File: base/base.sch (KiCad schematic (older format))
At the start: 22 parts, among them J1 USB_OTG, SW1 SW_Push, U1 Z80CPU, U2 27C256, U3 7404, U4 55257, U5 7432, U6 16550, U7 FT230XS, X1 4 MHz

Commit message: Layout work
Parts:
- added J2: CONN_02X20, Pin_Headers:Pin_Header_Straight_2x20_Pitch2.54mm, symbol CONN_02X20
- added unit 4 of U3
- added unit 3 of U5
- added X2: 1.8432 MHz, Oscillators:Oscillator_DIP-8, symbol CXO_DIP8
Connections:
- net labels added: IORQ, UART_CE
- wire segments 161 -> 223
- no-connect marks 2 -> 4
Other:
- moved on the sheet: C3, D1, R1, SW1, U3A, U3B

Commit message: Replaced SMD passives with THT
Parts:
- C1, C2, C4, C5, C6, C7, C8: footprint Capacitors_SMD:C_0805 -> Capacitors_THT:C_Disc_D4.3mm_W1.9mm_P5.00mm
- C3: footprint Capacitors_SMD:CP_Elec_4x4.5 -> Capacitors_THT:CP_Radial_D5.0mm_P2.50mm
- D1: footprint Diodes_SMD:D_SOD-523 -> Diodes_THT:D_A-405_P7.62mm_Horizontal
- R1, R2, R3: footprint Resistors_SMD:R_0805 -> Resistors_THT:R_Axial_DIN0207_L6.3mm_D2.5mm_P10.16mm_Horizontal
- SW1: footprint Buttons_Switches_SMD:SW_SPST_TL3342 -> Buttons_Switches_THT:SW_PUSH_6mm_h5mm
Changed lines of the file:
@@
 F 0 "C1" H 2592 2246 50  0000 L CNN
 F 1 "1 uF" H 2592 2155 50  0000 L CNN
-F 2 "Capacitors_SMD:C_0805" H 2500 2200 50  0001 C CNN
+F 2 "Capacitors_THT:C_Disc_D4.3mm_W1.9mm_P5.00mm" H 2500 2200 50  0001 C CNN
 F 3 "" H 2500 2200 50  0001 C CNN
 	1    2500 2200
@@
 F 0 "C2" H 5342 2396 50  0000 L CNN
 F 1 "1 uF" H 5342 2305 50  0000 L CNN
-F 2 "Capacitors_SMD:C_0805" H 5250 2350 50  0001 C CNN
+F 2 "Capacitors_THT:C_Disc_D4.3mm_W1.9mm_P5.00mm" H 5250 2350 50  0001 C CNN
 F 3 "" H 5250 2350 50  0001 C CNN
 	1    5250 2350
@@
 F 0 "SW1" H 1000 10585 50  0000 C CNN
 F 1 "SW_Push" H 1000 10494 50  0000 C CNN
-F 2 "Buttons_Switches_SMD:SW_SPST_TL3342" H 1000 10500 50  0001 C CNN
+F 2 "Buttons_Switches_THT:SW_PUSH_6mm_h5mm" H 1000 10500 50  0001 C CNN
 F 3 "" H 1000 10500 50  0001 C CNN
 	1    1000 10300
@@
 F 0 "R1" H 1559 9996 50  0000 L CNN
 F 1 "10k" H 1559 9905 50  0000 L CNN
-F 2 "Resistors_SMD:R_0805" H 1500 9950 50  0001 C CNN
+F 2 "Resistors_THT:R_Axial_DIN0207_L6.3mm_D2.5mm_P10.16mm_Horizontal" H 1500 9950 50  0001 C CNN
 F 3 "" H 1500 9950 50  0001 C CNN
 	1    1500 9950
@@
 F 0 "C3" H 1291 10596 50  0000 L CNN
 F 1 "47 uF" H 1291 10505 50  0000 L CNN
-F 2 "Capacitors_SMD:CP_Elec_4x4.5" H 1200 10550 50  0001 C CNN
+F 2 "Capacitors_THT:CP_Radial_D5.0mm_P2.50mm" H 1200 10550 50  0001 C CNN
 F 3 "" H 1200 10550 50  0001 C CNN
 	1    1200 10550
@@
 F 0 "C4" H 7592 2446 50  0000 L CNN
 F 1 "1 uF" H 7592 2355 50  0000 L CNN
-F 2 "Capacitors_SMD:C_0805" H 7500 2400 50  0001 C CNN
+F 2 "Capacitors_THT:C_Disc_D4.3mm_W1.9mm_P5.00mm" H 7500 2400 50  0001 C CNN
 F 3 "" H 7500 2400 50  0001 C CNN
 	1    7500 2400
@@
 F 0 "C5" H 9892 2346 50  0000 L CNN
 F 1 "C_Small" H 9892 2255 50  0000 L CNN
-F 2 "Capacitors_SMD:C_0805" H 9800 2300 50  0001 C CNN
+F 2 "Capacitors_THT:C_Disc_D4.3mm_W1.9mm_P5.00mm" H 9800 2300 50  0001 C CNN
 F 3 "" H 9800 2300 50  0001 C CNN
 	1    9800 2300
@@
 F 0 "D1" H 1350 9484 50  0000 C CNN
 F 1 "1N4148" H 1350 9575 50  0000 C CNN
-F 2 "Diodes_SMD:D_SOD-523" H 1350 9525 50  0001 C CNN
+F 2 "Diodes_THT:D_A-405_P7.62mm_Horizontal" H 1350 9525 50  0001 C CNN
 F 3 "" H 1350 9700 50  0001 C CNN
 	1    1350 9700
@@
 F 0 "R2" V 12700 3050 50  0000 C CNN
 F 1 "27" V 12700 3200 50  0000 C CNN
-F 2 "Resistors_SMD:R_0805" H 12800 3100 50  0001 C CNN
+F 2 "Resistors_THT:R_Axial_DIN0207_L6.3mm_D2.5mm_P10.16mm_Horizontal" H 12800 3100 50  0001 C CNN
 F 3 "" H 12800 3100 50  0001 C CNN
 	1    12800 3100
@@
 F 0 "R3" V 12700 3250 50  0000 C CNN
 F 1 "27" V 12700 3100 50  0000 C CNN
-F 2 "Resistors_SMD:R_0805" H 12800 3200 50  0001 C CNN
+F 2 "Resistors_THT:R_Axial_DIN0207_L6.3mm_D2.5mm_P10.16mm_Horizontal" H 12800 3200 50  0001 C CNN
 F 3 "" H 12800 3200 50  0001 C CNN
 	1    12800 3200
@@
 F 0 "C8" V 12621 2800 50  0000 C CNN
 F 1 "100 nF" V 12712 2800 50  0000 C CNN
-F 2 "Capacitors_SMD:C_0805" H 12850 2800 50  0001 C CNN
+F 2 "Capacitors_THT:C_Disc_D4.3mm_W1.9mm_P5.00mm" H 12850 2800 50  0001 C CNN
 F 3 "" H 12850 2800 50  0001 C CNN
 	1    12850 2800
@@
 F 0 "C6" H 12492 3496 50  0000 L CNN
 F 1 "47 nF" H 12492 3405 50  0000 L CNN
-F 2 "Capacitors_SMD:C_0805" H 12400 3450 50  0001 C CNN
+F 2 "Capacitors_THT:C_Disc_D4.3mm_W1.9mm_P5.00mm" H 12400 3450 50  0001 C CNN
 F 3 "" H 12400 3450 50  0001 C CNN
 	1    12400 3450
@@
 F 0 "C7" H 12692 3496 50  0000 L CNN
 F 1 "47 nF" H 12692 3405 50  0000 L CNN
-F 2 "Capacitors_SMD:C_0805" H 12600 3450 50  0001 C CNN
+F 2 "Capacitors_THT:C_Disc_D4.3mm_W1.9mm_P5.00mm" H 12600 3450 50  0001 C CNN
 F 3 "" H 12600 3450 50  0001 C CNN
 	1    12600 3450

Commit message: Further layout work
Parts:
- removed C2, C4: 1 uF, Capacitors_THT:C_Disc_D4.3mm_W1.9mm_P5.00mm, symbol C_Small
- removed C6, C7: 47 nF, Capacitors_THT:C_Disc_D4.3mm_W1.9mm_P5.00mm, symbol C_Small
- removed C8: 100 nF, Capacitors_THT:C_Disc_D4.3mm_W1.9mm_P5.00mm, symbol C_Small
- removed J1: USB_OTG, Connectors_USB:USB_Micro-B_Molex-105017-0001, symbol USB_OTG
- removed J2: CONN_02X20, Pin_Headers:Pin_Header_Straight_2x20_Pitch2.54mm, symbol CONN_02X20
- removed R2, R3: 27, Resistors_THT:R_Axial_DIN0207_L6.3mm_D2.5mm_P10.16mm_Horizontal, symbol R_Small
- removed U7: FT230XS, SMD_Packages:SO-16-L, symbol FT230XS
- added J1: FTDI, symbol CONN_01X06
- added JP1: CLK JMP, symbol Jumper_NC_Small
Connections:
- net labels added: CTS, INT, RTS, RX, TX
- wire segments 223 -> 174
- no-connect marks 4 -> 3

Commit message: Added RC2014 header to schematic
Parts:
- added J?: CONN_01X40, symbol CONN_01X40
- added J?: CONN_01X04, symbol CONN_01X04
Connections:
- net +5V: now also J?.18 (P18)
- net A0: now also J?.16 (P16)
- net A1: now also J?.15 (P15)
- net A10: now also J?.6 (P6)
- net A11: now also J?.5 (P5)
- net A12: now also J?.4 (P4)
- net A13: now also J?.3 (P3)
- net A14: now also J?.2 (P2)
- net A15: now also J?.1 (P1)
- net A2: now also J?.14 (P14)
- net A3: now also J?.13 (P13)
- net A4: now also J?.12 (P12)
- net A5: now also J?.11 (P11)
- net A6: now also J?.10 (P10)
- net A7: now also J?.9 (P9)
- net A8: now also J?.8 (P8)
- net A9: now also J?.7 (P7)
- net D0: now also J?.27 (P27)
- net D1: now also J?.28 (P28)
- net D2: now also J?.29 (P29)
- net D3: now also J?.30 (P30)
- net D4: now also J?.31 (P31)
- net D5: now also J?.32 (P32)
- net D6: now also J?.33 (P33)
- net D7: now also J?.34 (P34)
- net GND: now also J?.17 (P17)
- net INT: now also J?.22 (P22)
- net IORQ: now also J?.26 (P26)
- net MREQ: now also J?.23 (P23)
- net RD: now also J?.25 (P25)
- net RESET: now also J?.20 (P20)
- net RX: now also J?.36 (P36)
- net TX: now also J?.35 (P35)
- net WR: now also J?.24 (P24)
- net M1: now reaches U1.27 (~M1~)
- net M1: now also J?.19 (P19)
- net CLOCK: now reaches JP1.2, U1.6 (~CLK~)
- net CLOCK: now also J?.21 (P21)
- new net: J?.37 (P37), J?.4 (P4)
- new net: J?.3 (P3), J?.38 (P38)
- new net: J?.2 (P2), J?.39 (P39)
- new net: J?.1 (P1), J?.40 (P40)
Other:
- moved on the sheet: C3, D1, R1, SW1, U3A, U3B

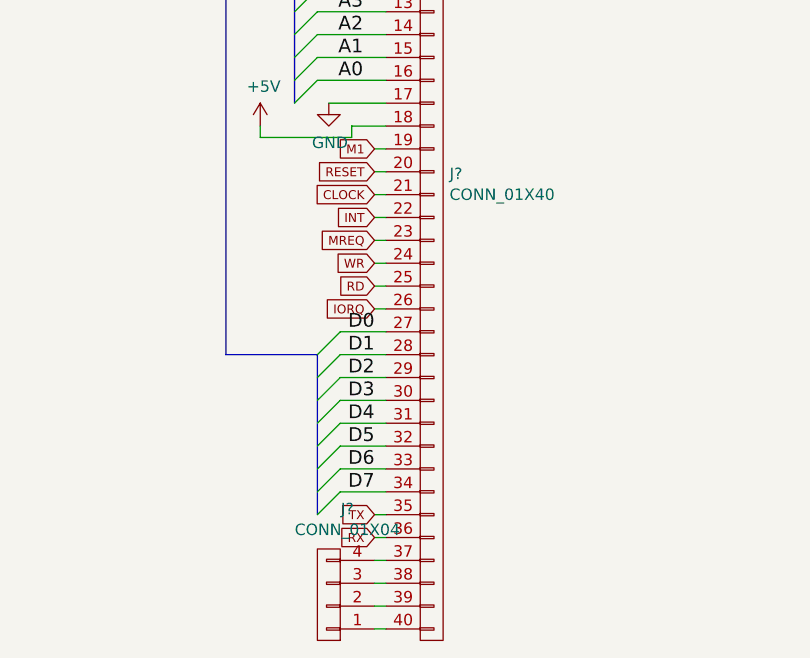
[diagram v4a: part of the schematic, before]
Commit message: Changed FTDI and CLK_JMP footprint
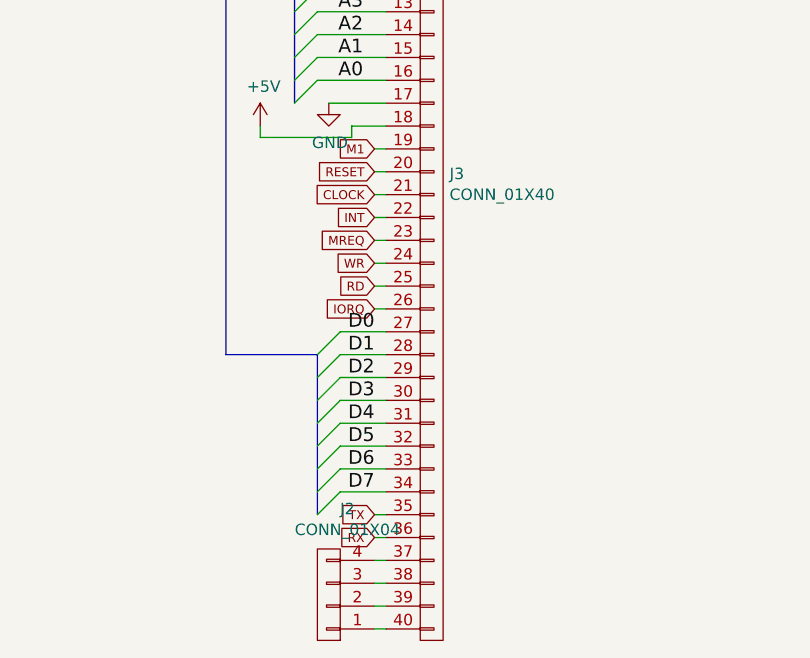
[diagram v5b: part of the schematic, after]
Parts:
- J1: footprint (none) -> Pin_Headers:Pin_Header_Straight_1x06_Pitch2.54mm
- J2: renamed from J?; footprint (none) -> Pin_Headers:Pin_Header_Straight_1x04_Pitch2.54mm
- J3: renamed from J?; footprint (none) -> Pin_Headers:Pin_Header_Straight_1x40_Pitch2.54mm
- JP1: footprint (none) -> Pin_Headers:Pin_Header_Straight_1x02_Pitch2.54mm
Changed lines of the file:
@@
 	6150 3350 6250 3450
 $Comp
-L GND #PWR9
+L GND #PWR01
 U 1 1 5966AA78
 P 2500 5500
-F 0 "#PWR9" H 2500 5250 50  0001 C CNN
+F 0 "#PWR01" H 2500 5250 50  0001 C CNN
 F 1 "GND" H 2505 5327 50  0000 C CNN
 F 2 "" H 2500 5500 50  0001 C CNN
@@
 $EndComp
 $Comp
-L +5V #PWR8
+L +5V #PWR02
 U 1 1 5966ABCC
 P 2500 2000
-F 0 "#PWR8" H 2500 1850 50  0001 C CNN
+F 0 "#PWR02" H 2500 1850 50  0001 C CNN
 F 1 "+5V" H 2515 2173 50  0000 C CNN
 F 2 "" H 2500 2000 50  0001 C CNN
@@
 $EndComp
 $Comp
-L GND #PWR11
+L GND #PWR03
 U 1 1 5966AD0D
 P 5250 4650
-F 0 "#PWR11" H 5250 4400 50  0001 C CNN
+F 0 "#PWR03" H 5250 4400 50  0001 C CNN
 F 1 "GND" H 5255 4477 50  0000 C CNN
 F 2 "" H 5250 4650 50  0001 C CNN
@@
 $EndComp
 $Comp
-L +5V #PWR10
+L +5V #PWR04
 U 1 1 5966ADF6
 P 5250 2150
-F 0 "#PWR10" H 5250 2000 50  0001 C CNN
+F 0 "#PWR04" H 5250 2000 50  0001 C CNN
 F 1 "+5V" H 5265 2323 50  0000 C CNN
 F 2 "" H 5250 2150 50  0001 C CNN
@@
 $EndComp
 $Comp
-L +5V #PWR2
+L +5V #PWR05
 U 1 1 5966B631
 P 950 2600
-F 0 "#PWR2" H 950 2450 50  0001 C CNN
+F 0 "#PWR05" H 950 2450 50  0001 C CNN
 F 1 "+5V" H 965 2773 50  0000 C CNN
 F 2 "" H 950 2600 50  0001 C CNN
@@
 NoConn ~ 650  3000
 $Comp
-L GND #PWR3
+L GND #PWR06
 U 1 1 5966B6FC
 P 950 3400
-F 0 "#PWR3" H 950 3150 50  0001 C CNN
+F 0 "#PWR06" H 950 3150 50  0001 C CNN
 F 1 "GND" H 955 3227 50  0000 C CNN
 F 2 "" H 950 3400 50  0001 C CNN
@@
 $EndComp
 $Comp
-L GND #PWR1
+L GND #PWR07
 U 1 1 5966D26A
 P 12150 8950
-F 0 "#PWR1" H 12150 8700 50  0001 C CNN
+F 0 "#PWR07" H 12150 8700 50  0001 C CNN
 F 1 "GND" H 12155 8777 50  0000 C CNN
 F 2 "" H 12150 8950 50  0001 C CNN
@@
 $EndComp
 $Comp
-L +5V #PWR5
+L +5V #PWR08
 U 1 1 5966D324
 P 13050 8150
-F 0 "#PWR5" H 13050 8000 50  0001 C CNN
+F 0 "#PWR08" H 13050 8000 50  0001 C CNN
 F 1 "+5V" H 13065 8323 50  0000 C CNN
 F 2 "" H 13050 8150 50  0001 C CNN
@@
 ~RESET~
 $Comp
-L GND #PWR4
+L GND #PWR09
 U 1 1 5966DD94
 P 12650 9300
-F 0 "#PWR4" H 12650 9050 50  0001 C CNN
+F 0 "#PWR09" H 12650 9050 50  0001 C CNN
 F 1 "GND" H 12655 9127 50  0000 C CNN
 F 2 "" H 12650 9300 50  0001 C CNN
@@
 $EndComp
 $Comp
-L GND #PWR7
+L GND #PWR010
 U 1 1 5966E3B1
 P 13500 9200
-F 0 "#PWR7" H 13500 8950 50  0001 C CNN
+F 0 "#PWR010" H 13500 8950 50  0001 C CNN
 F 1 "GND" H 13505 9027 50  0000 C CNN
 F 2 "" H 13500 9200 50  0001 C CNN
@@
 $EndComp
 $Comp
-L +5V #PWR6
+L +5V #PWR011
 U 1 1 5966E548
 P 13500 8500
-F 0 "#PWR6" H 13500 8350 50  0001 C CNN
+F 0 "#PWR011" H 13500 8350 50  0001 C CNN
 F 1 "+5V" H 13515 8673 50  0000 C CNN
 F 2 "" H 13500 8500 50  0001 C CNN
@@
 $EndComp
 $Comp
-L +5V #PWR12
+L +5V #PWR012
 U 1 1 5967000D
 P 7500 2200
-F 0 "#PWR12" H 7500 2050 50  0001 C CNN
+F 0 "#PWR012" H 7500 2050 50  0001 C CNN
 F 1 "+5V" H 7515 2373 50  0000 C CNN
 F 2 "" H 7500 2200 50  0001 C CNN
@@
 $EndComp
 $Comp
-L GND #PWR13
+L GND #PWR013
 U 1 1 5967079F
 P 7500 4700
-F 0 "#PWR13" H 7500 4450 50  0001 C CNN
+F 0 "#PWR013" H 7500 4450 50  0001 C CNN
 F 1 "GND" H 7505 4527 50  0000 C CNN
 F 2 "" H 7500 4700 50  0001 C CNN
@@
 $EndComp
 $Comp
-L +5V #PWR18
+L +5V #PWR014
 U 1 1 5967680A
 P 9800 2100
-F 0 "#PWR18" H 9800 1950 50  0001 C CNN
+F 0 "#PWR014" H 9800 1950 50  0001 C CNN
 F 1 "+5V" H 9815 2273 50  0000 C CNN
 F 2 "" H 9800 2100 50  0001 C CNN
@@
 $EndComp
 $Comp
-L GND #PWR19
+L GND #PWR015
 U 1 1 59676BF3
 P 9800 6000
-F 0 "#PWR19" H 9800 5750 50  0001 C CNN
+F 0 "#PWR015" H 9800 5750 50  0001 C CNN
 F 1 "GND" H 9805 5827 50  0000 C CNN
 F 2 "" H 9800 6000 50  0001 C CNN
@@
 NoConn ~ 8800 4700
 $Comp
-L +5V #PWR16
+L +5V #PWR016
 U 1 1 596A671B
 P 8300 3950
-F 0 "#PWR16" H 8300 3800 50  0001 C CNN
+F 0 "#PWR016" H 8300 3800 50  0001 C CNN
 F 1 "+5V" H 8315 4123 50  0000 C CNN
 F 2 "" H 8300 3950 50  0001 C CNN
@@
 $EndComp
 $Comp
-L +5V #PWR14
+L +5V #PWR017
 U 1 1 596A8FB6
 P 7650 5700
-F 0 "#PWR14" H 7650 5550 50  0001 C CNN
+F 0 "#PWR017" H 7650 5550 50  0001 C CNN
 F 1 "+5V" H 7665 5873 50  0000 C CNN
 F 2 "" H 7650 5700 50  0001 C CNN
@@
 NoConn ~ 7350 6100
 $Comp
-L GND #PWR15
+L GND #PWR018
 U 1 1 596A8FBD
 P 7650 6500
-F 0 "#PWR15" H 7650 6250 50  0001 C CNN
+F 0 "#PWR018" H 7650 6250 50  0001 C CNN
 F 1 "GND" H 7655 6327 50  0000 C CNN
 F 2 "" H 7650 6500 50  0001 C CNN
@@
 A15
 $Comp
-L GND #PWR17
+L GND #PWR019
 U 1 1 596AAB37
 P 8450 5550
-F 0 "#PWR17" H 8450 5300 50  0001 C CNN
+F 0 "#PWR019" H 8450 5300 50  0001 C CNN
 F 1 "GND" H 8455 5377 50  0000 C CNN
 F 2 "" H 8450 5550 50  0001 C CNN
@@
 F 0 "JP1" H 1500 3212 50  0000 C CNN
 F 1 "CLK JMP" H 1500 3121 50  0000 C CNN
-F 2 "" H 1500 3000 50  0001 C CNN
+F 2 "Pin_Headers:Pin_Header_Straight_1x02_Pitch2.54mm" H 1500 3000 50  0001 C CNN
 F 3 "" H 1500 3000 50  0001 C CNN
 	1    1500 3000
@@
 F 0 "J1" H 11369 2575 50  0000 C CNN
 F 1 "FTDI" H 11369 2666 50  0000 C CNN
-F 2 "" H 11450 3050 50  0001 C CNN
+F 2 "Pin_Headers:Pin_Header_Straight_1x06_Pitch2.54mm" H 11450 3050 50  0001 C CNN
 F 3 "" H 11450 3050 50  0001 C CNN
 	1    11450 3050
@@
 $EndComp
 $Comp
-L GND #PWR20
+L GND #PWR020
 U 1 1 5987A0C1
 P 11750 3400
-F 0 "#PWR20" H 11750 3150 50  0001 C CNN
+F 0 "#PWR020" H 11750 3150 50  0001 C CNN
 F 1 "GND" H 11755 3227 50  0000 C CNN
 F 2 "" H 11750 3400 50  0001 C CNN
@@
 TX
 $Comp
-L +5V #PWR21
+L +5V #PWR021
 U 1 1 5987AEFD
 P 12050 2950
-F 0 "#PWR21" H 12050 2800 50  0001 C CNN
+F 0 "#PWR021" H 12050 2800 50  0001 C CNN
 F 1 "+5V" H 12065 3123 50  0000 C CNN
 F 2 "" H 12050 2950 50  0001 C CNN
@@
 INT
 $Comp
-L CONN_01X40 J?
+L CONN_01X40 J3
 U 1 1 59F61B61
 P 6400 8100
-F 0 "J?" H 6478 8141 50  0000 L CNN
+F 0 "J3" H 6478 8141 50  0000 L CNN
 F 1 "CONN_01X40" H 6478 8050 50  0000 L CNN
-F 2 "" H 6400 8100 50  0001 C CNN
+F 2 "Pin_Headers:Pin_Header_Straight_1x40_Pitch2.54mm" H 6400 8100 50  0001 C CNN
 F 3 "" H 6400 8100 50  0001 C CNN
 	1    6400 8100
@@
 	5800 7750 5900 7650
 $Comp
-L GND #PWR?
+L GND #PWR022
 U 1 1 59F6444E
 P 5950 7750
-F 0 "#PWR?" H 5950 7500 50  0001 C CNN
+F 0 "#PWR022" H 5950 7500 50  0001 C CNN
 F 1 "GND" H 5955 7577 50  0000 C CNN
 F 2 "" H 5950 7750 50  0001 C CNN
@@
 $EndComp
 $Comp
-L +5V #PWR?
+L +5V #PWR023
 U 1 1 59F6487C
 P 5650 7850
-F 0 "#PWR?" H 5650 7700 50  0001 C CNN
+F 0 "#PWR023" H 5650 7700 50  0001 C CNN
 F 1 "+5V" H 5665 8023 50  0000 C CNN
 F 2 "" H 5650 7850 50  0001 C CNN
@@
 RX
 $Comp
-L CONN_01X04 J?
+L CONN_01X04 J2
 U 1 1 59F6B8B8
 P 5950 9900
-F 0 "J?" H 5869 9525 50  0000 C CNN
+F 0 "J2" H 5869 9525 50  0000 C CNN
 F 1 "CONN_01X04" H 5869 9616 50  0000 C CNN
-F 2 "" H 5950 9900 50  0001 C CNN
+F 2 "Pin_Headers:Pin_Header_Straight_1x04_Pitch2.54mm" H 5950 9900 50  0001 C CNN
 F 3 "" H 5950 9900 50  0001 C CNN
 	1    5950 9900

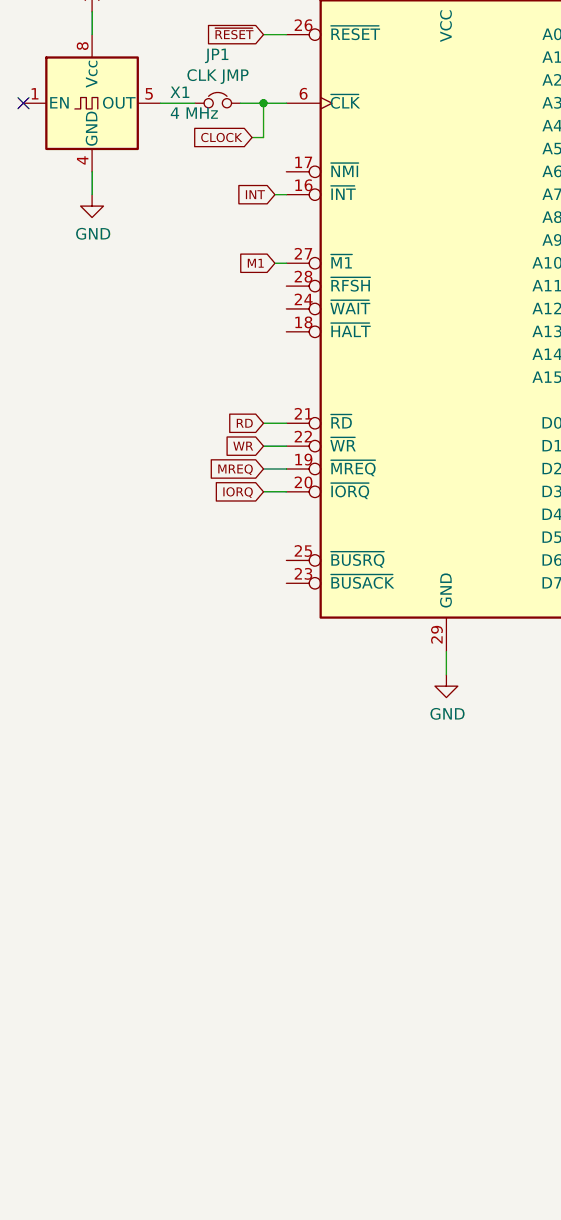
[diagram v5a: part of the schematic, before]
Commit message: Broke out remaining z80 pins
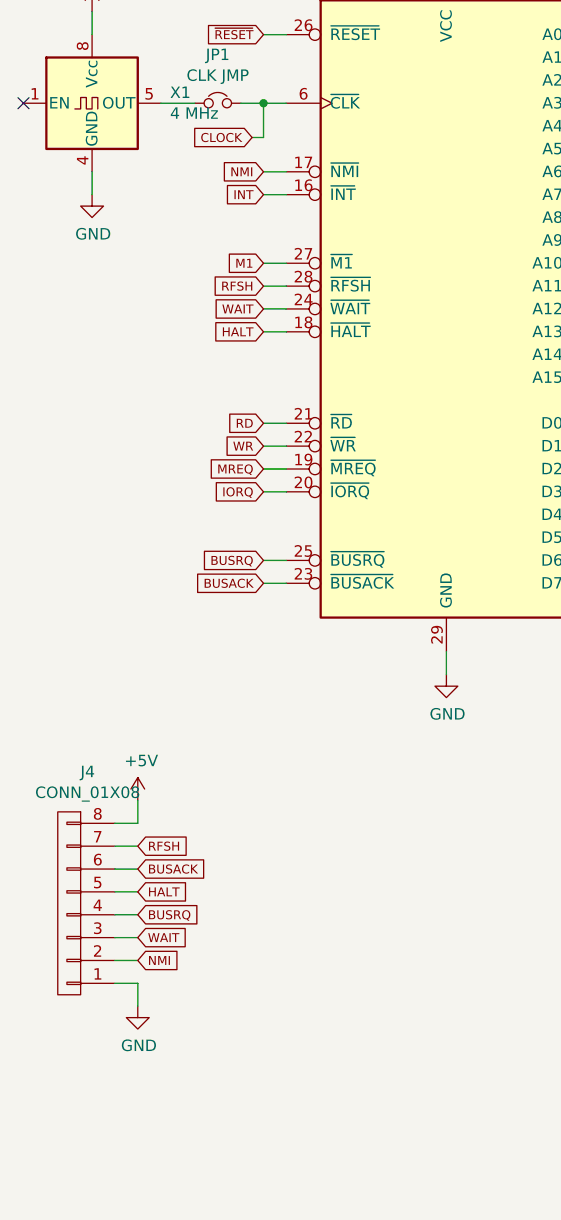
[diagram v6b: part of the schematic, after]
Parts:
- added J4: CONN_01X08, Pin_Headers:Pin_Header_Straight_1x08_Pitch2.54mm, symbol CONN_01X08
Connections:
- net +5V: now also J4.8 (P8)
- net GND: now also J4.1 (P1)
- net NMI: now reaches U1.17 (~NMI~)
- net NMI: now also J4.2 (P2)
- net HALT: now reaches U1.18 (~HALT~)
- net HALT: now also J4.5 (P5)
- net BUSACK: now reaches U1.23 (~BUSACK~)
- net BUSACK: now also J4.6 (P6)
- net WAIT: now reaches U1.24 (~WAIT~)
- net WAIT: now also J4.3 (P3)
- net BUSRQ: now reaches U1.25 (~BUSRQ~)
- net BUSRQ: now also J4.4 (P4)
- net RFSH: now reaches U1.28 (~RFSH~)
- net RFSH: now also J4.7 (P7)
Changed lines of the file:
@@
 Text GLabel 8750 5500 0    39   Input ~ 0
 INT
-Text GLabel 1750 3400 0    39   Input ~ 0
+Text GLabel 1700 3400 0    39   Input ~ 0
 INT
 $Comp
@@
 Text GLabel 1650 3150 0    39   Input ~ 0
 CLOCK
-Text GLabel 1750 3700 0    39   Input ~ 0
+Text GLabel 1700 3700 0    39   Input ~ 0
 M1
 Text GLabel 6150 8250 0    39   Input ~ 0
@@
 	8750 5500 8800 5500
 Wire Wire Line
-	1750 3400 1800 3400
+	1700 3400 1800 3400
 Wire Wire Line
 	5900 6250 6200 6250
@@
 Connection ~ 1700 3000
 Wire Wire Line
-	1750 3700 1800 3700
+	1700 3700 1800 3700
 Wire Wire Line
 	6150 8250 6200 8250
@@
 Wire Bus Line
 	5500 5250 5450 5250
+$Comp
+L CONN_01X08 J4
+U 1 1 59FF87B1
+P 850 6500
+F 0 "J4" H 769 5925 50  0000 C CNN
+F 1 "CONN_01X08" H 769 6016 50  0000 C CNN
+F 2 "Pin_Headers:Pin_Header_Straight_1x08_Pitch2.54mm" H 850 6500 50  0001 C CNN
+F 3 "" H 850 6500 50  0001 C CNN
+	1    850  6500
+	-1   0    0    1
+$EndComp
+$Comp
+L GND #PWR024
+U 1 1 59FF89E4
+P 1150 6950
+F 0 "#PWR024" H 1150 6700 50  0001 C CNN
+F 1 "GND" H 1155 6777 50  0000 C CNN
+F 2 "" H 1150 6950 50  0001 C CNN
+F 3 "" H 1150 6950 50  0001 C CNN
+	1    1150 6950
+	1    0    0    -1
+$EndComp
+Wire Wire Line
+	1050 6850 1150 6850
+Wire Wire Line
+	1150 6850 1150 6950
+$Comp
+L +5V #PWR025
+U 1 1 59FF8B42
+P 1150 6050
+F 0 "#PWR025" H 1150 5900 50  0001 C CNN
+F 1 "+5V" H 1165 6223 50  0000 C CNN
+F 2 "" H 1150 6050 50  0001 C CNN
+F 3 "" H 1150 6050 50  0001 C CNN
+	1    1150 6050
+	1    0    0    -1
+$EndComp
+Wire Wire Line
+	1050 6150 1150 6150
+Wire Wire Line
+	1150 6150 1150 6050
+Text GLabel 1700 5100 0    39   Input ~ 0
+BUSACK
+Wire Wire Line
+	1700 5100 1800 5100
+Text GLabel 1700 5000 0    39   Input ~ 0
+BUSRQ
+Wire Wire Line
+	1700 5000 1800 5000
+Text GLabel 1700 4000 0    39   Input ~ 0
+HALT
+Wire Wire Line
+	1700 4000 1800 4000
+Text GLabel 1700 3900 0    39   Input ~ 0
+WAIT
+Wire Wire Line
+	1700 3900 1800 3900
+Text GLabel 1700 3800 0    39   Input ~ 0
+RFSH
+Wire Wire Line
+	1700 3800 1800 3800
+Text GLabel 1700 3300 0    39   Input ~ 0
+NMI
+Wire Wire Line
+	1700 3300 1800 3300
+Text GLabel 1150 6250 2    39   Input ~ 0
+RFSH
+Wire Wire Line
+	1150 6250 1050 6250
+Text GLabel 1150 6350 2    39   Input ~ 0
+BUSACK
+Text GLabel 1150 6450 2    39   Input ~ 0
+HALT
+Text GLabel 1150 6550 2    39   Input ~ 0
+BUSRQ
+Text GLabel 1150 6650 2    39   Input ~ 0
+WAIT
+Text GLabel 1150 6750 2    39   Input ~ 0
+NMI
+Wire Wire Line
+	1150 6750 1050 6750
+Wire Wire Line
+	1150 6650 1050 6650
+Wire Wire Line
+	1150 6550 1050 6550
+Wire Wire Line
+	1150 6450 1050 6450
+Wire Wire Line
+	1150 6350 1050 6350
 $EndSCHEMATC
